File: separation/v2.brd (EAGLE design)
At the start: 43.2 x 22.9 mm, 8 parts

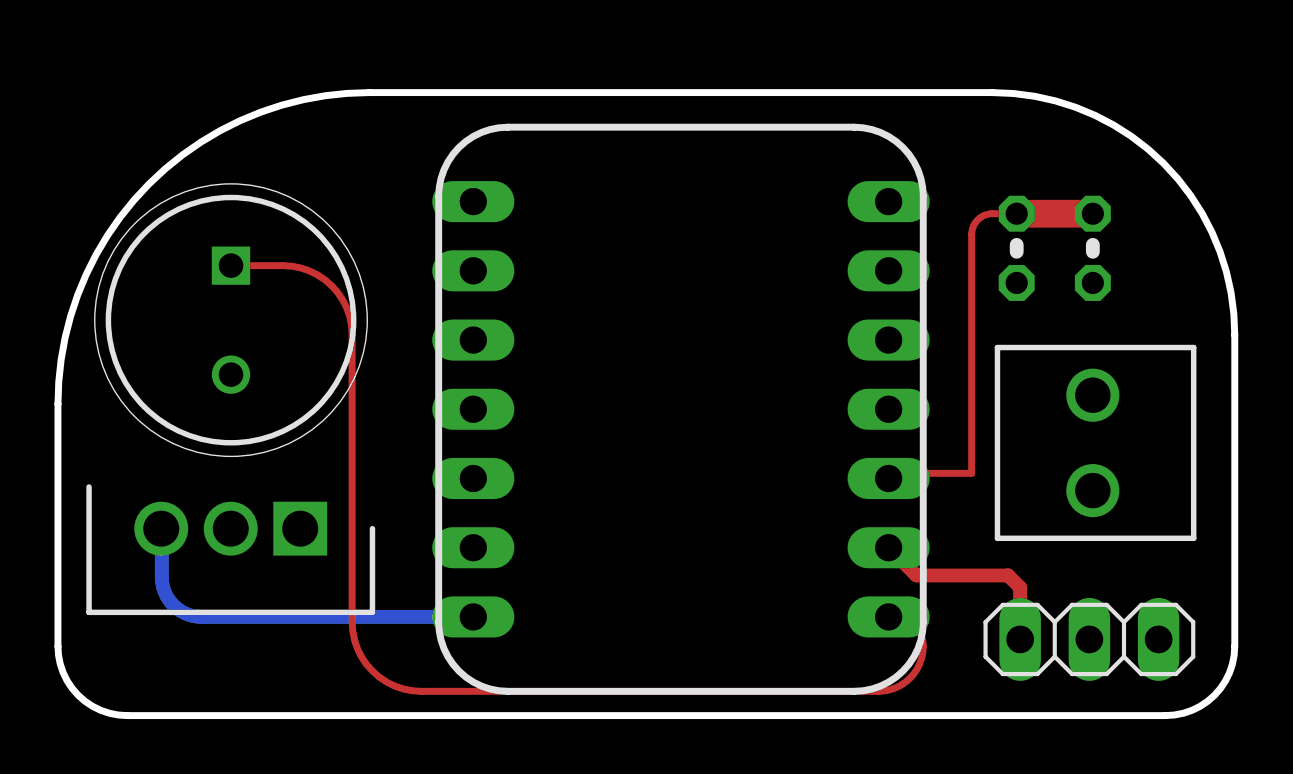
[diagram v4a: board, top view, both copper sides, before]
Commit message: make corners symmetrical
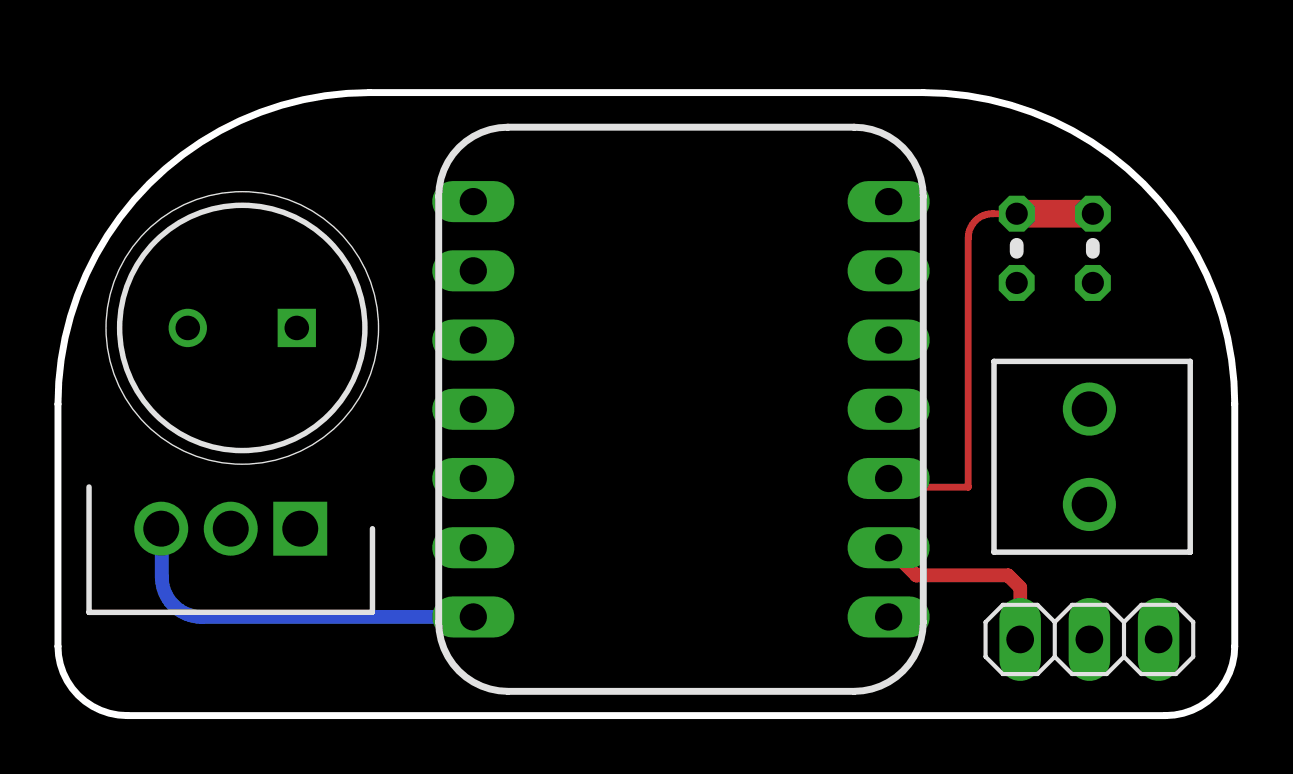
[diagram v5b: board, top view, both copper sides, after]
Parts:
- moved LOUD 3.32 mm to (-15.4, 24.4), turned to 180 degrees
- moved BAT 0.52 mm to (13.7, 17.9)
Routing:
- net BUZZ: track 40.3 -> 0.00 mm
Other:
- outline, holes or cut-outs redrawn
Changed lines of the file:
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@@
 <wire x1="-8.89" y1="26.543" x2="-10.668" y2="26.543" width="1.524" layer="29"/>
 <wire x1="-8.89" y1="29.083" x2="-10.668" y2="29.083" width="1.524" layer="29"/>
-<wire x1="-12.7" y1="33.02" x2="-24.13" y2="21.59" width="0.254" layer="20" curve="90"/>
 <wire x1="-24.13" y1="21.59" x2="-24.13" y2="12.7" width="0.254" layer="20"/>
 <wire x1="-24.13" y1="12.7" x2="-21.59" y2="10.16" width="0.254" layer="20" curve="90"/>
 <wire x1="-21.59" y1="10.16" x2="16.51" y2="10.16" width="0.254" layer="20"/>
 <wire x1="16.51" y1="10.16" x2="19.05" y2="12.7" width="0.254" layer="20" curve="90"/>
-<wire x1="19.05" y1="12.7" x2="19.05" y2="24.13" width="0.254" layer="20"/>
-<wire x1="10.16" y1="33.02" x2="19.05" y2="24.13" width="0.254" layer="20" curve="-90"/>
-<wire x1="10.16" y1="33.02" x2="-12.7" y2="33.02" width="0.254" layer="20"/>
+<wire x1="19.05" y1="21.59" x2="7.62" y2="33.02" width="0.254" layer="20" curve="90"/>
+<wire x1="7.62" y1="33.02" x2="-12.7" y2="33.02" width="0.254" layer="20"/>
+<wire x1="-24.13" y1="21.59" x2="-12.7" y2="33.02" width="0.254" layer="20" curve="-90"/>
+<wire x1="19.05" y1="12.7" x2="19.05" y2="21.59" width="0.254" layer="20"/>
 </plain>
 <attributes>
@@
 <attribute name="VALUE" x="-12.065" y="30.2895" size="0.4064" layer="27" ratio="10" rot="R270"/>
 </element>
-<element name="LOUD" library="SamacSys_Parts" package="CAPPRD400W70D900H500" package3d_urn="urn:adsk.eagle:package:34276129/2" value="KSTG931AP" x="-17.78" y="26.67" smashed="yes" rot="R270">
-<attribute name="DESCRIPTION" value="RS PRO 4V Electromagnetic Buzzer, 92dB" x="-17.78" y="26.67" size="1.778" layer="27" font="vector" ratio="15" rot="R270" display="off"/>
-<attribute name="HEIGHT" value="5mm" x="-17.78" y="26.67" size="1.778" layer="27" font="vector" ratio="15" rot="R270" display="off"/>
-<attribute name="MANUFACTURER_NAME" value="RS Components" x="-17.78" y="26.67" size="1.778" layer="27" font="vector" ratio="15" rot="R270" display="off"/>
-<attribute name="MANUFACTURER_PART_NUMBER" value="KSTG931AP" x="-17.78" y="26.67" size="1.778" layer="27" font="vector" ratio="15" rot="R270" display="off"/>
-<attribute name="RS_PART_NUMBER" value="" x="-17.78" y="26.67" size="1.778" layer="27" font="vector" ratio="15" rot="R270" display="off"/>
-<attribute name="RS_PRICE-STOCK" value="" x="-17.78" y="26.67" size="1.778" layer="27" font="vector" ratio="15" rot="R270" display="off"/>
+<element name="LOUD" library="SamacSys_Parts" package="CAPPRD400W70D900H500" package3d_urn="urn:adsk.eagle:package:34276129/2" value="KSTG931AP" x="-15.367" y="24.384" smashed="yes" rot="R180">
+<attribute name="DESCRIPTION" value="RS PRO 4V Electromagnetic Buzzer, 92dB" x="-15.367" y="24.384" size="1.778" layer="27" font="vector" ratio="15" rot="R180" display="off"/>
+<attribute name="HEIGHT" value="5mm" x="-15.367" y="24.384" size="1.778" layer="27" font="vector" ratio="15" rot="R180" display="off"/>
+<attribute name="MANUFACTURER_NAME" value="RS Components" x="-15.367" y="24.384" size="1.778" layer="27" font="vector" ratio="15" rot="R180" display="off"/>
+<attribute name="MANUFACTURER_PART_NUMBER" value="KSTG931AP" x="-15.367" y="24.384" size="1.778" layer="27" font="vector" ratio="15" rot="R180" display="off"/>
+<attribute name="RS_PART_NUMBER" value="" x="-15.367" y="24.384" size="1.778" layer="27" font="vector" ratio="15" rot="R180" display="off"/>
+<attribute name="RS_PRICE-STOCK" value="" x="-15.367" y="24.384" size="1.778" layer="27" font="vector" ratio="15" rot="R180" display="off"/>
 </element>
 <element name="LDO" library="SamacSys_Parts" package="TO255P460X1020X2008-3P" package3d_urn="urn:adsk.eagle:package:34276127/2" value="L7805ACV" x="-15.24" y="17.018" smashed="yes" rot="R180">
@@
 <attribute name="RS_PRICE-STOCK" value="http://uk.rs-online.com/web/p/products/2988508P" x="-15.24" y="17.018" size="1.778" layer="27" font="vector" ratio="15" rot="R180" display="off"/>
 </element>
-<element name="BAT" library="SamacSys_Parts" package="MB332350M02SZ" value="MB332-350M02SZ" x="13.843" y="18.415" smashed="yes" rot="R90">
-<attribute name="DESCRIPTION" value="RS PRO 3.5mm Pitch Straight, PCB Terminal Block, Through Hole, 2 Way" x="13.843" y="18.415" size="1.778" layer="27" font="vector" ratio="15" rot="R90" display="off"/>
-<attribute name="HEIGHT" value="12.76mm" x="13.843" y="18.415" size="1.778" layer="27" font="vector" ratio="15" rot="R90" display="off"/>
-<attribute name="MANUFACTURER_NAME" value="RS Components" x="13.843" y="18.415" size="1.778" layer="27" font="vector" ratio="15" rot="R90" display="off"/>
-<attribute name="MANUFACTURER_PART_NUMBER" value="MB332-350M02SZ" x="13.843" y="18.415" size="1.778" layer="27" font="vector" ratio="15" rot="R90" display="off"/>
-<attribute name="RS_PART_NUMBER" value="7901149" x="13.843" y="18.415" size="1.778" layer="27" font="vector" ratio="15" rot="R90" display="off"/>
-<attribute name="RS_PRICE-STOCK" value="https://uk.rs-online.com/web/p/products/7901149" x="13.843" y="18.415" size="1.778" layer="27" font="vector" ratio="15" rot="R90" display="off"/>
+<element name="BAT" library="SamacSys_Parts" package="MB332350M02SZ" value="MB332-350M02SZ" x="13.716" y="17.907" smashed="yes" rot="R90">
+<attribute name="DESCRIPTION" value="RS PRO 3.5mm Pitch Straight, PCB Terminal Block, Through Hole, 2 Way" x="13.716" y="17.907" size="1.778" layer="27" font="vector" ratio="15" rot="R90" display="off"/>
+<attribute name="HEIGHT" value="12.76mm" x="13.716" y="17.907" size="1.778" layer="27" font="vector" ratio="15" rot="R90" display="off"/>
+<attribute name="MANUFACTURER_NAME" value="RS Components" x="13.716" y="17.907" size="1.778" layer="27" font="vector" ratio="15" rot="R90" display="off"/>
+<attribute name="MANUFACTURER_PART_NUMBER" value="MB332-350M02SZ" x="13.716" y="17.907" size="1.778" layer="27" font="vector" ratio="15" rot="R90" display="off"/>
+<attribute name="RS_PART_NUMBER" value="7901149" x="13.716" y="17.907" size="1.778" layer="27" font="vector" ratio="15" rot="R90" display="off"/>
+<attribute name="RS_PRICE-STOCK" value="https://uk.rs-online.com/web/p/products/7901149" x="13.716" y="17.907" size="1.778" layer="27" font="vector" ratio="15" rot="R90" display="off"/>
 </element>
 <element name="SERCON" library="pinhead" library_urn="urn:adsk.eagle:library:325" package="1X03" package3d_urn="urn:adsk.eagle:package:22458/2" value="" x="13.716" y="12.954" smashed="yes" rot="R180">
@@
 <contactref element="LOUD" pad="2"/>
 <contactref element="R2" pad="2"/>
-<wire x1="13.716" y1="12.954" x2="13.843" y2="21.915" width="0" layer="19" extent="1-1"/>
+<wire x1="13.716" y1="12.954" x2="13.716" y2="21.407" width="0" layer="19" extent="1-1"/>
 <wire x1="-17.79" y1="17.018" x2="13.716" y2="12.954" width="0" layer="19" extent="1-1"/>
-<wire x1="-17.78" y1="22.67" x2="-17.79" y2="17.018" width="0" layer="19" extent="1-1"/>
-<wire x1="11.049" y1="26.035" x2="-17.78" y2="22.67" width="0" layer="19" extent="1-1"/>
+<wire x1="-19.367" y1="24.384" x2="-17.79" y2="17.018" width="0" layer="19" extent="1-1"/>
+<wire x1="11.049" y1="26.035" x2="-19.367" y2="24.384" width="0" layer="19" extent="1-1"/>
 <wire x1="-8.89" y1="16.3195" x2="11.049" y2="26.035" width="0" layer="19" extent="1-1"/>
 </signal>
@@
 <contactref element="LDO" pad="1"/>
 <contactref element="R1" pad="1"/>
-<wire x1="16.256" y1="12.954" x2="13.843" y2="18.415" width="0" layer="19" extent="1-1"/>
+<wire x1="16.256" y1="12.954" x2="13.716" y2="17.907" width="0" layer="19" extent="1-1"/>
 <wire x1="-15.24" y1="17.018" x2="16.256" y2="12.954" width="0" layer="19" extent="1-1"/>
 <wire x1="13.843" y1="26.035" x2="-15.24" y2="17.018" width="0" layer="19" extent="1-1"/>
@@
 <signal name="BUZZ">
 <contactref element="LOUD" pad="1"/>
-<wire x1="-13.335" y1="13.589" x2="-10.795" y2="11.049" width="0.254" layer="1" curve="90"/>
-<wire x1="-13.335" y1="24.13" x2="-15.875" y2="26.67" width="0.254" layer="1" curve="90"/>
-<wire x1="-15.875" y1="26.67" x2="-17.78" y2="26.67" width="0.254" layer="1"/>
-<wire x1="-13.335" y1="13.589" x2="-13.335" y2="24.13" width="0.254" layer="1"/>
-<wire x1="-10.795" y1="11.049" x2="-2.54" y2="11.049" width="0.254" layer="1"/>
-<wire x1="-2.54" y1="11.049" x2="5.969" y2="11.049" width="0.254" layer="1"/>
-<wire x1="5.969" y1="11.049" x2="7.62" y2="12.7" width="0.254" layer="1" curve="90"/>
-<wire x1="7.62" y1="12.7" x2="6.5405" y2="13.7795" width="0.254" layer="1" curve="90"/>
 <contactref element="MCU-R" pad="3"/>
-<wire x1="-17.78" y1="26.67" x2="-8.89" y2="23.9395" width="0" layer="19" extent="1-1"/>
+<wire x1="-15.367" y1="24.384" x2="-8.89" y2="23.9395" width="0" layer="19" extent="1-1"/>
 </signal>
 <signal name="VSENSE">
@@
 <wire x1="11.049" y1="28.575" x2="13.843" y2="28.575" width="1.016" layer="1"/>
 <wire x1="11.049" y1="28.575" x2="10.16" y2="28.575" width="0.254" layer="1"/>
-<wire x1="10.16" y1="28.575" x2="9.398" y2="27.813" width="0.254" layer="1" curve="90"/>
-<wire x1="9.398" y1="19.05" x2="6.5405" y2="19.05" width="0.254" layer="1"/>
-<wire x1="6.5405" y1="19.05" x2="6.35" y2="18.8595" width="0.254" layer="1" curve="90"/>
-<wire x1="9.398" y1="27.813" x2="9.398" y2="19.05" width="0.254" layer="1"/>
+<wire x1="10.16" y1="28.575" x2="9.271" y2="27.686" width="0.254" layer="1" curve="90"/>
+<wire x1="6.35" y1="18.8595" x2="6.6675" y2="18.542" width="0.254" layer="1"/>
+<wire x1="9.271" y1="18.542" x2="6.6675" y2="18.542" width="0.254" layer="1"/>
+<wire x1="9.271" y1="27.686" x2="9.271" y2="18.542" width="0.254" layer="1"/>
 </signal>
 <signal name="A0">

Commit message: rotate regulator
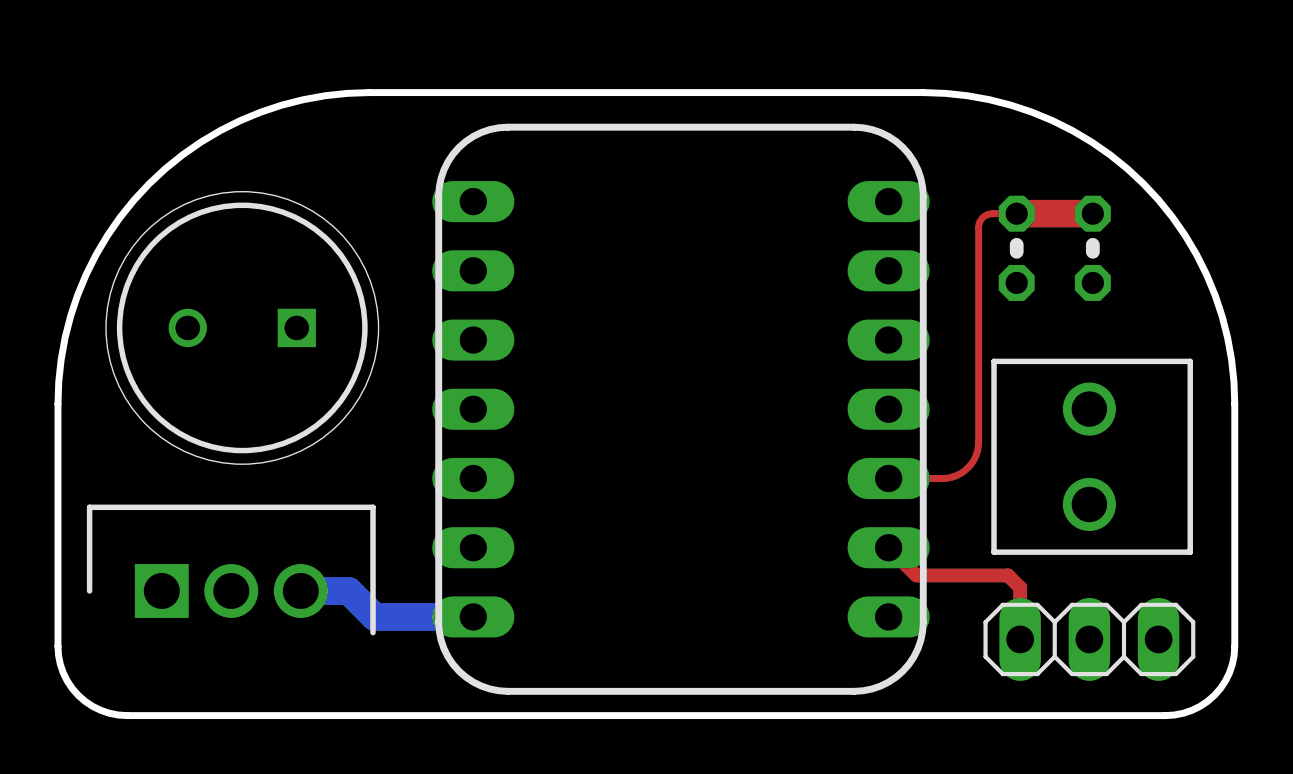
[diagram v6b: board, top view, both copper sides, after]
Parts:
- moved LDO 5.57 mm to (-20.3, 14.7), turned to 0 degrees
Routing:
- net VCC: track 13.8 -> 6.72 mm
- net VSENSE: track 17.1 -> 16.1 mm
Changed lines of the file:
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@@
 <attribute name="RS_PRICE-STOCK" value="" x="-15.367" y="24.384" size="1.778" layer="27" font="vector" ratio="15" rot="R180" display="off"/>
 </element>
-<element name="LDO" library="SamacSys_Parts" package="TO255P460X1020X2008-3P" package3d_urn="urn:adsk.eagle:package:34276127/2" value="L7805ACV" x="-15.24" y="17.018" smashed="yes" rot="R180">
-<attribute name="ALLIED_NUMBER" value="70013701" x="-15.24" y="17.018" size="1.778" layer="27" font="vector" ratio="15" rot="R180" display="off"/>
-<attribute name="DESCRIPTION" value="Linear voltage regulator,L7805ACV 5V 1A STMicroelectronics L7805ACV, Single Linear Voltage Regulator, 1A 5 V, 2%, 3-Pin TO-220" x="-15.24" y="17.018" size="1.778" layer="27" font="vector" ratio="15" rot="R180" display="off"/>
-<attribute name="HEIGHT" value="4.6mm" x="-15.24" y="17.018" size="1.778" layer="27" font="vector" ratio="15" rot="R180" display="off"/>
-<attribute name="MANUFACTURER_NAME" value="STMicroelectronics" x="-15.24" y="17.018" size="1.778" layer="27" font="vector" ratio="15" rot="R180" display="off"/>
-<attribute name="MANUFACTURER_PART_NUMBER" value="L7805ACV" x="-15.24" y="17.018" size="1.778" layer="27" font="vector" ratio="15" rot="R180" display="off"/>
-<attribute name="RS_PART_NUMBER" value="2988508P" x="-15.24" y="17.018" size="1.778" layer="27" font="vector" ratio="15" rot="R180" display="off"/>
-<attribute name="RS_PRICE-STOCK" value="http://uk.rs-online.com/web/p/products/2988508P" x="-15.24" y="17.018" size="1.778" layer="27" font="vector" ratio="15" rot="R180" display="off"/>
+<element name="LDO" library="SamacSys_Parts" package="TO255P460X1020X2008-3P" package3d_urn="urn:adsk.eagle:package:34276127/2" value="L7805ACV" x="-20.32" y="14.732" smashed="yes">
+<attribute name="ALLIED_NUMBER" value="70013701" x="-20.32" y="14.732" size="1.778" layer="27" font="vector" ratio="15" display="off"/>
+<attribute name="DESCRIPTION" value="Linear voltage regulator,L7805ACV 5V 1A STMicroelectronics L7805ACV, Single Linear Voltage Regulator, 1A 5 V, 2%, 3-Pin TO-220" x="-20.32" y="14.732" size="1.778" layer="27" font="vector" ratio="15" display="off"/>
+<attribute name="HEIGHT" value="4.6mm" x="-20.32" y="14.732" size="1.778" layer="27" font="vector" ratio="15" display="off"/>
+<attribute name="MANUFACTURER_NAME" value="STMicroelectronics" x="-20.32" y="14.732" size="1.778" layer="27" font="vector" ratio="15" display="off"/>
+<attribute name="MANUFACTURER_PART_NUMBER" value="L7805ACV" x="-20.32" y="14.732" size="1.778" layer="27" font="vector" ratio="15" display="off"/>
+<attribute name="RS_PART_NUMBER" value="2988508P" x="-20.32" y="14.732" size="1.778" layer="27" font="vector" ratio="15" display="off"/>
+<attribute name="RS_PRICE-STOCK" value="http://uk.rs-online.com/web/p/products/2988508P" x="-20.32" y="14.732" size="1.778" layer="27" font="vector" ratio="15" display="off"/>
 </element>
 <element name="BAT" library="SamacSys_Parts" package="MB332350M02SZ" value="MB332-350M02SZ" x="13.716" y="17.907" smashed="yes" rot="R90">
@@
 <contactref element="R2" pad="2"/>
 <wire x1="13.716" y1="12.954" x2="13.716" y2="21.407" width="0" layer="19" extent="1-1"/>
-<wire x1="-17.79" y1="17.018" x2="13.716" y2="12.954" width="0" layer="19" extent="1-1"/>
-<wire x1="-19.367" y1="24.384" x2="-17.79" y2="17.018" width="0" layer="19" extent="1-1"/>
+<wire x1="-17.77" y1="14.732" x2="13.716" y2="12.954" width="0" layer="19" extent="1-1"/>
+<wire x1="-19.367" y1="24.384" x2="-17.77" y2="14.732" width="0" layer="19" extent="1-1"/>
 <wire x1="11.049" y1="26.035" x2="-19.367" y2="24.384" width="0" layer="19" extent="1-1"/>
 <wire x1="-8.89" y1="16.3195" x2="11.049" y2="26.035" width="0" layer="19" extent="1-1"/>
@@
 <contactref element="MCU-R" pad="7"/>
 <contactref element="LDO" pad="3"/>
-<wire x1="-20.34" y1="17.018" x2="-20.32" y2="16.998" width="0.508" layer="16" curve="-90"/>
-<wire x1="-20.32" y1="16.998" x2="-20.32" y2="15.24" width="0.508" layer="16"/>
-<wire x1="-20.32" y1="15.24" x2="-18.8595" y2="13.7795" width="0.508" layer="16" curve="90"/>
-<wire x1="-18.8595" y1="13.7795" x2="-8.89" y2="13.7795" width="0.508" layer="16"/>
+<wire x1="-15.22" y1="14.732" x2="-13.462" y2="14.732" width="1.016" layer="16"/>
+<wire x1="-12.5095" y1="13.7795" x2="-8.89" y2="13.7795" width="1.016" layer="16"/>
+<wire x1="-13.462" y1="14.732" x2="-12.5095" y2="13.7795" width="1.016" layer="16"/>
 </signal>
 <signal name="+3V3">
@@
 <contactref element="R1" pad="1"/>
 <wire x1="16.256" y1="12.954" x2="13.716" y2="17.907" width="0" layer="19" extent="1-1"/>
-<wire x1="-15.24" y1="17.018" x2="16.256" y2="12.954" width="0" layer="19" extent="1-1"/>
-<wire x1="13.843" y1="26.035" x2="-15.24" y2="17.018" width="0" layer="19" extent="1-1"/>
+<wire x1="-20.32" y1="14.732" x2="16.256" y2="12.954" width="0" layer="19" extent="1-1"/>
+<wire x1="13.843" y1="26.035" x2="-20.32" y2="14.732" width="0" layer="19" extent="1-1"/>
 </signal>
 <signal name="SERVO">
@@
 <wire x1="11.049" y1="28.575" x2="13.843" y2="28.575" width="1.016" layer="1"/>
 <wire x1="11.049" y1="28.575" x2="10.16" y2="28.575" width="0.254" layer="1"/>
-<wire x1="10.16" y1="28.575" x2="9.271" y2="27.686" width="0.254" layer="1" curve="90"/>
-<wire x1="6.35" y1="18.8595" x2="6.6675" y2="18.542" width="0.254" layer="1"/>
-<wire x1="9.271" y1="18.542" x2="6.6675" y2="18.542" width="0.254" layer="1"/>
-<wire x1="9.271" y1="27.686" x2="9.271" y2="18.542" width="0.254" layer="1"/>
+<wire x1="6.35" y1="18.8595" x2="8.3185" y2="18.8595" width="0.254" layer="1"/>
+<wire x1="8.3185" y1="18.8595" x2="9.652" y2="20.193" width="0.254" layer="1" curve="90"/>
+<wire x1="9.652" y1="20.193" x2="9.652" y2="28.067" width="0.254" layer="1"/>
+<wire x1="9.652" y1="28.067" x2="10.16" y2="28.575" width="0.254" layer="1" curve="-90"/>
 </signal>
 <signal name="A0">
